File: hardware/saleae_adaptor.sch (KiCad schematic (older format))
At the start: 18 parts, among them J1 Conn_01x12, J2 Conn_02x05_Odd_Even

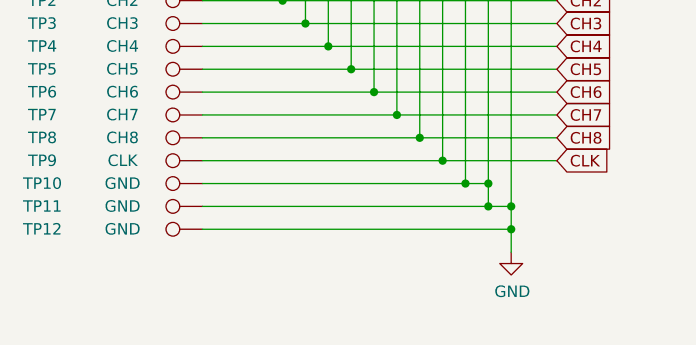
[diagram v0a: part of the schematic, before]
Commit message: Added new GND pad
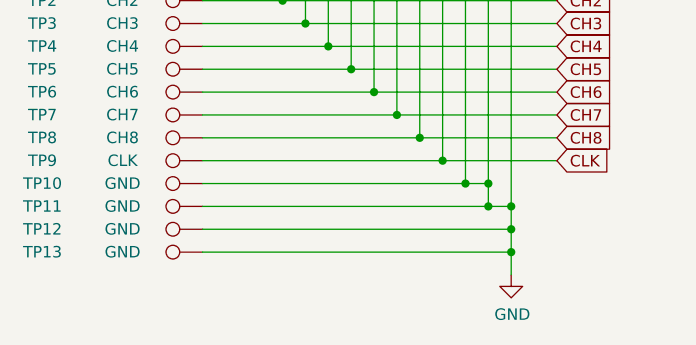
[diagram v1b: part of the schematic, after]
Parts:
- added TP13: GND, TestPoint:TestPoint_Pad_4.0x4.0mm, symbol Connector:TestPoint
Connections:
- net GND: now also TP13.1
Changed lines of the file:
@@
 L power:GND #PWR01
 U 1 1 5F966915
-P 6000 5100
-F 0 "#PWR01" H 6000 4850 50  0001 C CNN
-F 1 "GND" H 6005 4927 50  0000 C CNN
-F 2 "" H 6000 5100 50  0001 C CNN
-F 3 "" H 6000 5100 50  0001 C CNN
-	1    6000 5100
+P 6000 5200
+F 0 "#PWR01" H 6000 4950 50  0001 C CNN
+F 1 "GND" H 6005 5027 50  0000 C CNN
+F 2 "" H 6000 5200 50  0001 C CNN
+F 3 "" H 6000 5200 50  0001 C CNN
+	1    6000 5200
 	1    0    0    -1
 $EndComp
@@
 	8750 3650 8750 3600
 Connection ~ 8750 3600
+$Comp
+L Connector:TestPoint TP13
+U 1 1 5F94AE77
+P 4650 5100
+F 0 "TP13" V 4650 5800 50  0000 C CNN
+F 1 "GND" V 4650 5450 50  0000 C CNN
+F 2 "TestPoint:TestPoint_Pad_4.0x4.0mm" H 4850 5100 50  0001 C CNN
+F 3 "~" H 4850 5100 50  0001 C CNN
+	1    4650 5100
+	0    -1   -1   0
+$EndComp
+Wire Wire Line
+	4650 5100 6000 5100
+Wire Wire Line
+	6000 5200 6000 5100
+Connection ~ 6000 5100
 $EndSCHEMATC
